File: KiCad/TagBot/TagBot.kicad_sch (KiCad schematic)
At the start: 51 parts, among them IC101 ADXL343BCCZ-RL, J101 Conn_ST_STDC14, J102 Conn_01x06, J103 Conn_01x02, J104 Conn_01x06, J105 Conn_01x02, J106 Conn_01x08, J107 Conn_01x03, J108 Conn_01x03, J109 Conn_01x03, J110 Conn_01x03, J111 Conn_01x04, SW101 SW_Push, SW102 SW_Push, SW103 SW_SPDT_312, U101 STM32G431CBUx, Y101 Crystal

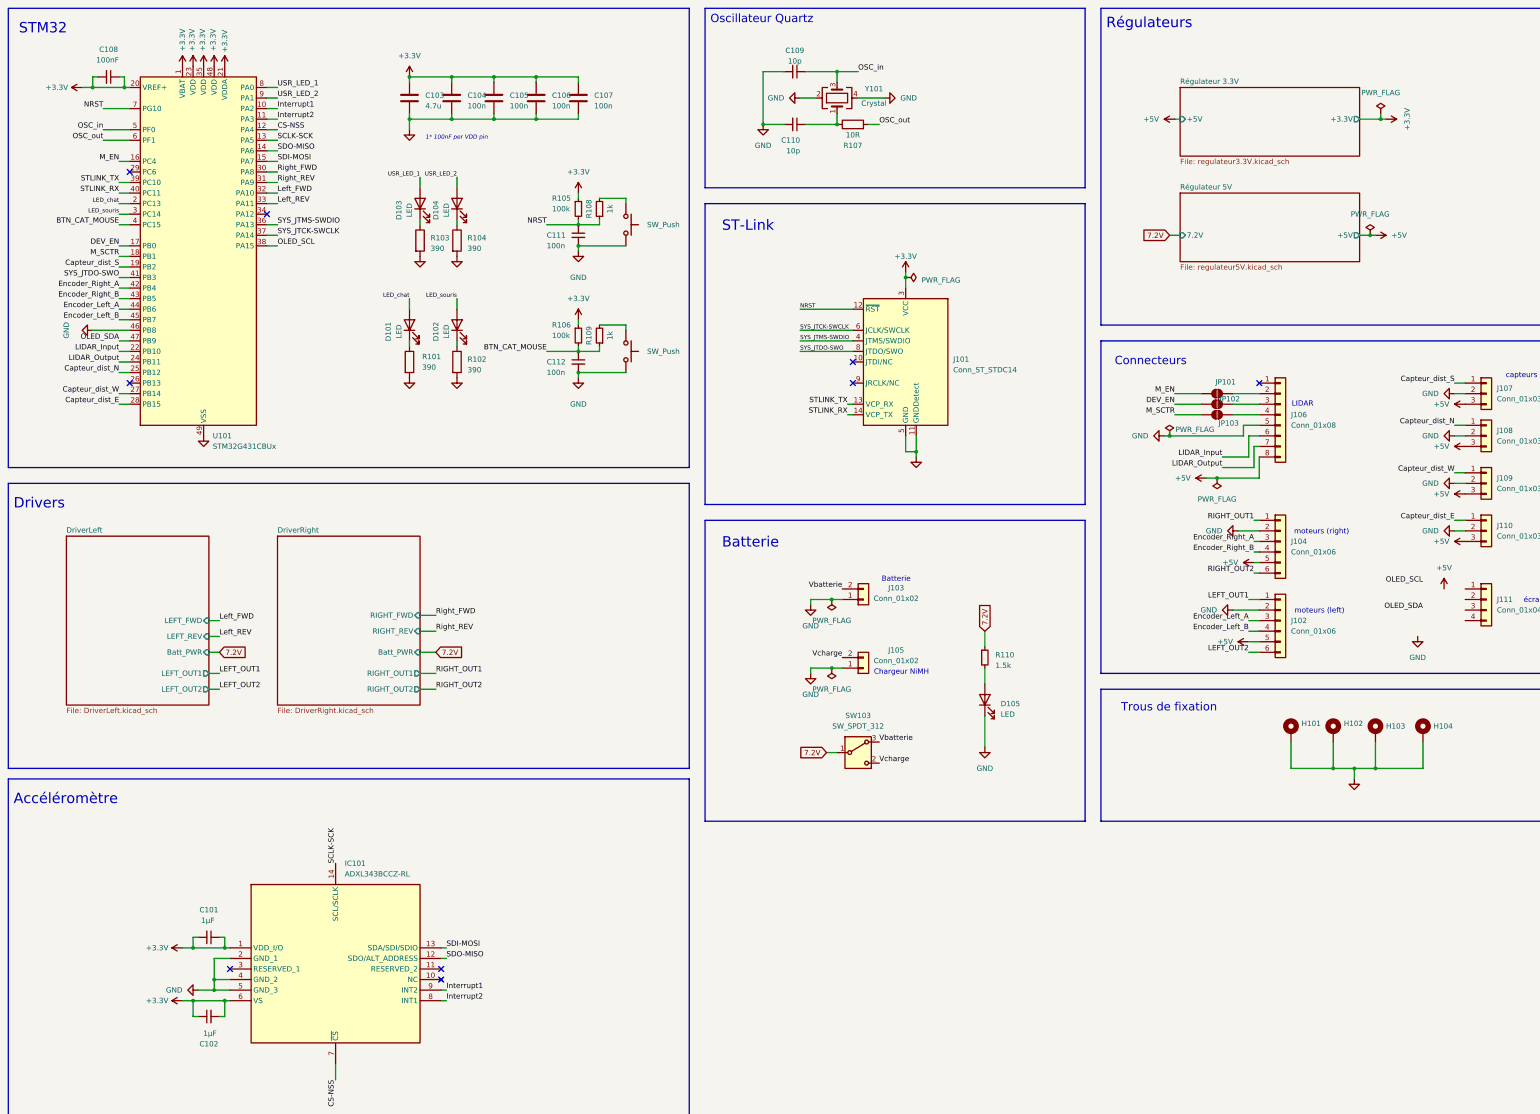
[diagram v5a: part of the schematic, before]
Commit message: update footprint kicad
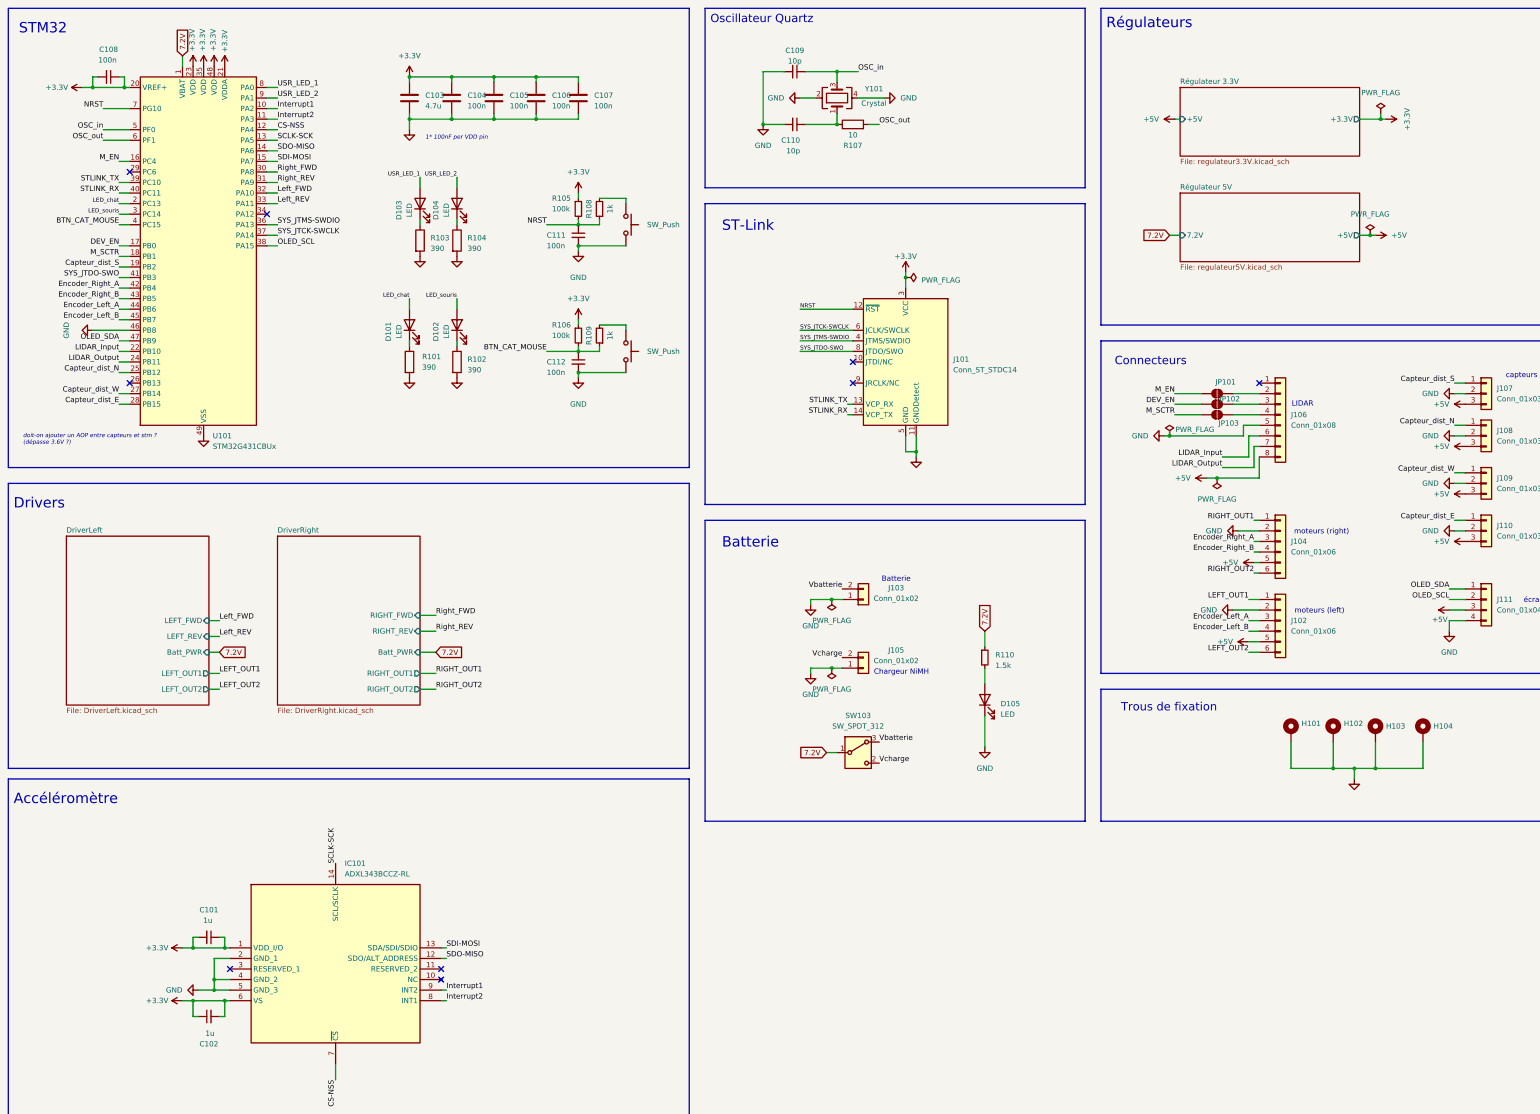
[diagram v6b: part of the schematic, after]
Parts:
- C101, C102: value 1µF -> 1u; footprint (none) -> Capacitor_SMD:C_0402_1005Metric
- C108: value 100nF -> 100n; footprint (none) -> Capacitor_SMD:C_0402_1005Metric
- IC101: footprint ADXL343BCCZRL -> ADXL343BCCZ-RL:ADXL343BCCZRL
- J102, J104: footprint (none) -> Connector_JST:JST_XH_B6B-XH-A_1x06_P2.50mm_Vertical
- J103, J105: footprint Connector_AMASS:AMASS_XT60-F_1x02_P7.20mm_Vertical -> Connector_JST:JST_XH_B2B-XH-A_1x02_P2.50mm_Vertical
- J106: footprint (none) -> Connector_JST:JST_XH_B8B-XH-A_1x08_P2.50mm_Vertical
- J107, J108, J109, J110: footprint (none) -> Connector_JST:JST_XH_B3B-XH-A_1x03_P2.50mm_Vertical
- J111: footprint (none) -> Connector_JST:JST_XH_B4B-XH-A_1x04_P2.50mm_Vertical
- JP101, JP102, JP103: footprint (none) -> Jumper:SolderJumper-2_P1.3mm_Open_TrianglePad1.0x1.5mm
- R107: value 10R -> 10
- SW103: footprint (none) -> wurth_472121020311:472121020311
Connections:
- net +3.3V: no longer U101.1 (VBAT)
- net +5V: now also J111.3 (Pin_3)
- net 7.2V: now also U101.1 (VBAT)
- net GND: now also J111.4 (Pin_4)
- net OLED_SCL: now also J111.2 (Pin_2)
- net OLED_SDA: now also J111.1 (Pin_1)
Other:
- note added: "doit-on ajouter un AOP entre capteurs et stm ? (dépasse 3.6V ?)"
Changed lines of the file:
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@@
 	(wire
 		(pts
+			(xy 361.95 157.48) (xy 365.76 157.48)
+		)
+		(stroke
+			(width 0)
+			(type default)
+		)
+	)
+	(wire
+		(pts
 			(xy 313.69 162.56) (xy 316.23 162.56)
 		)
@@
 	(wire
 		(pts
+			(xy 361.95 160.02) (xy 365.76 160.02)
+		)
+		(stroke
+			(width 0)
+			(type default)
+		)
+	)
+	(wire
+		(pts
 			(xy 132.08 41.91) (xy 132.08 40.64)
 		)
@@
 	(wire
 		(pts
+			(xy 361.95 162.56) (xy 361.95 165.1)
+		)
+		(stroke
+			(width 0)
+			(type default)
+		)
+	)
+	(wire
+		(pts
 			(xy 213.36 157.48) (xy 215.9 157.48)
 		)
@@
 	(wire
 		(pts
+			(xy 57.15 26.67) (xy 57.15 29.21)
+		)
+		(stroke
+			(width 0)
+			(type default)
+		)
+	)
+	(wire
+		(pts
 			(xy 340.36 41.91) (xy 345.44 41.91)
 		)
@@
 	(wire
 		(pts
+			(xy 365.76 162.56) (xy 361.95 162.56)
+		)
+		(stroke
+			(width 0)
+			(type default)
+		)
+	)
+	(wire
+		(pts
 			(xy 363.22 129.54) (xy 365.76 129.54)
 		)
@@
 	(wire
 		(pts
+			(xy 361.95 154.94) (xy 365.76 154.94)
+		)
+		(stroke
+			(width 0)
+			(type default)
+		)
+	)
+	(wire
+		(pts
 			(xy 205.74 92.71) (xy 218.44 92.71)
 		)
@@
 		)
 	)
+	(text "doit-on ajouter un AOP entre capteurs et stm ?\n(dépasse 3.6V ?)"
+		(exclude_from_sim no)
+		(at 18.796 120.396 0)
+		(effects
+			(font
+				(size 1 1)
+				(italic yes)
+			)
+			(justify left bottom)
+		)
+	)
 	(text "Batterie\n"
 		(exclude_from_sim no)
@@
 	)
 	(label "OLED_SCL"
-		(at 355.6 153.67 180)
+		(at 361.95 157.48 180)
 		(fields_autoplaced yes)
 		(effects
@@
 	)
 	(label "OLED_SDA"
-		(at 355.6 160.02 180)
+		(at 361.95 154.94 180)
 		(fields_autoplaced yes)
 		(effects
@@
 	(global_label "7.2V"
 		(shape input)
+		(at 57.15 26.67 90)
+		(fields_autoplaced yes)
+		(effects
+			(font
+				(size 1.27 1.27)
+			)
+			(justify left)
+		)
+		(property "Intersheetrefs" "${INTERSHEET_REFS}"
+			(at 57.15 19.5724 90)
+			(effects
+				(font
+					(size 1.27 1.27)
+				)
+				(justify left)
+				(hide yes)
+			)
+		)
+	)
+	(global_label "7.2V"
+		(shape input)
 		(at 294.64 69.85 180)
 		(fields_autoplaced yes)
@@
 			)
 		)
-		(property "Footprint" "Connector_AMASS:AMASS_XT60-F_1x02_P7.20mm_Vertical"
+		(property "Footprint" "Connector_JST:JST_XH_B2B-XH-A_1x02_P2.50mm_Vertical"
 			(at 220.98 157.48 0)
 			(effects
@@
 		(lib_name "GND_5")
 		(lib_id "power:GND")
-		(at 354.33 166.37 0)
+		(at 361.95 165.1 0)
 		(unit 1)
 		(exclude_from_sim no)
@@
 		(fields_autoplaced yes)
 		(property "Reference" "#PWR0148"
-			(at 354.33 172.72 0)
+			(at 361.95 171.45 0)
 			(effects
 				(font
@@
 		)
 		(property "Value" "GND"
-			(at 354.33 171.45 0)
+			(at 361.95 170.18 0)
 			(effects
 				(font
@@
 		)
 		(property "Footprint" ""
-			(at 354.33 166.37 0)
+			(at 361.95 165.1 0)
 			(effects
 				(font
@@
 		)
 		(property "Datasheet" ""
-			(at 354.33 166.37 0)
+			(at 361.95 165.1 0)
 			(effects
 				(font
@@
 		)
 		(property "Description" "Power symbol creates a global label with name \"GND\" , ground"
-			(at 354.33 166.37 0)
+			(at 361.95 165.1 0)
 			(effects
 				(font
@@
 			)
 		)
-		(property "Footprint" ""
+		(property "Footprint" "Connector_JST:JST_XH_B4B-XH-A_1x04_P2.50mm_Vertical"
 			(at 370.84 157.48 0)
 			(effects
@@
 			)
 		)
-		(property "Value" "1µF"
+		(property "Value" "1u"
 			(at 63.246 234.696 90)
 			(effects
@@
 			)
 		)
-		(property "Footprint" ""
+		(property "Footprint" "Capacitor_SMD:C_0402_1005Metric"
 			(at 63.5 238.76 0)
 			(effects
@@
 	(symbol
 		(lib_id "power:+5V")
-		(at 360.68 154.94 0)
+		(at 361.95 160.02 90)
 		(unit 1)
 		(exclude_from_sim no)
@@
 		(on_board yes)
 		(dnp no)
-		(fields_autoplaced yes)
 		(property "Reference" "#PWR0149"
-			(at 360.68 158.75 0)
+			(at 365.76 160.02 0)
 			(effects
 				(font
@@
 		)
 		(property "Value" "+5V"
-			(at 360.68 149.86 0)
+			(at 359.664 162.306 90)
 			(effects
 				(font
@@
 		)
 		(property "Footprint" ""
-			(at 360.68 154.94 0)
+			(at 361.95 160.02 0)
 			(effects
 				(font
@@
 		)
 		(property "Datasheet" ""
-			(at 360.68 154.94 0)
+			(at 361.95 160.02 0)
 			(effects
 				(font
@@
 		)
 		(property "Description" "Power symbol creates a global label with name \"+5V\""
-			(at 360.68 154.94 0)
+			(at 361.95 160.02 0)
 			(effects
 				(font
@@
 			)
 		)
-		(property "Value" "1µF"
+		(property "Value" "1u"
 			(at 63.754 261.874 90)
 			(effects
@@
 			)
 		)
-		(property "Footprint" ""
+		(property "Footprint" "Capacitor_SMD:C_0402_1005Metric"
 			(at 63.5 257.81 0)
 			(effects
@@
 			)
 		)
-		(property "Footprint" ""
+		(property "Footprint" "Jumper:SolderJumper-2_P1.3mm_Open_TrianglePad1.0x1.5mm"
 			(at 306.07 113.03 0)
 			(effects
@@
 			)
 		)
-		(property "Footprint" ""
+		(property "Footprint" "wurth_472121020311:472121020311"
 			(at 219.71 204.47 0)
 			(effects
@@
 	)
 	(symbol
-		(lib_name "+3.3V_1")
-		(lib_id "power:+3.3V")
-		(at 57.15 29.21 0)
-		(unit 1)
-		(exclude_from_sim no)
-		(in_bom yes)
-		(on_board yes)
-		(dnp no)
-		(property "Reference" "#PWR0102"
-			(at 57.15 33.02 0)
-			(effects
-				(font
-					(size 1.27 1.27)
-				)
-				(hide yes)
-			)
-		)
-		(property "Value" "+3.3V"
-			(at 57.15 22.86 90)
-			(effects
-				(font
-					(size 1.27 1.27)
-				)
-			)
-		)
-		(property "Footprint" ""
-			(at 57.15 29.21 0)
-			(effects
-				(font
-					(size 1.27 1.27)
-				)
-				(hide yes)
-			)
-		)
-		(property "Datasheet" ""
-			(at 57.15 29.21 0)
-			(effects
-				(font
-					(size 1.27 1.27)
-				)
-				(hide yes)
-			)
-		)
-		(property "Description" "Power symbol creates a global label with name \"+3.3V\""
-			(at 57.15 29.21 0)
-			(effects
-				(font
-					(size 1.27 1.27)
-				)
-				(hide yes)
-			)
-		)
-		(pin "1"
-		)
-		(instances
-			(project ""
-				(path "/6db08f37-7cb3-4000-93f1-ba0d0ffbeb19"
-					(reference "#PWR0102")
-					(unit 1)
-				)
-			)
-		)
-	)
-	(symbol
 		(lib_id "power:GND")
 		(at 250.19 193.04 0)
@@
 			)
 		)
-		(property "Footprint" ""
+		(property "Footprint" "Connector_JST:JST_XH_B8B-XH-A_1x08_P2.50mm_Vertical"
 			(at 321.31 113.03 0)
 			(effects
@@
 			)
 		)
-		(property "Footprint" "Connector_AMASS:AMASS_XT60-F_1x02_P7.20mm_Vertical"
+		(property "Footprint" "Connector_JST:JST_XH_B2B-XH-A_1x02_P2.50mm_Vertical"
 			(at 220.98 173.99 0)
 			(effects
@@
 			)
 		)
-		(property "Footprint" ""
+		(property "Footprint" "Jumper:SolderJumper-2_P1.3mm_Open_TrianglePad1.0x1.5mm"
 			(at 306.07 107.95 0)
 			(effects
@@
 			)
 		)
-		(property "Footprint" ""
+		(property "Footprint" "Connector_JST:JST_XH_B3B-XH-A_1x03_P2.50mm_Vertical"
 			(at 370.84 140.97 0)
 			(effects
@@
 			)
 		)
-		(property "Value" "100nF"
+		(property "Value" "100n"
 			(at 39.116 27.686 90)
 			(effects
@@
 			)
 		)
-		(property "Footprint" ""
+		(property "Footprint" "Capacitor_SMD:C_0402_1005Metric"
 			(at 39.37 31.75 0)
 			(effects
@@
 			)
 		)
-		(property "Footprint" ""
+		(property "Footprint" "Jumper:SolderJumper-2_P1.3mm_Open_TrianglePad1.0x1.5mm"
 			(at 306.07 110.49 0)
 			(effects
@@
 			)
 		)
-		(property "Footprint" ""
+		(property "Footprint" "Connector_JST:JST_XH_B3B-XH-A_1x03_P2.50mm_Vertical"
 			(at 370.84 107.95 0)
 			(effects
@@
 			)
 		)
-		(property "Value" "10R"
+		(property "Value" "10"
 			(at 218.44 45.72 90)
 			(effects
@@
 			)
 		)
-		(property "Footprint" ""
+		(property "Footprint" "Connector_JST:JST_XH_B6B-XH-A_1x06_P2.50mm_Vertical"
 			(at 321.31 162.56 0)
 			(effects
@@
 			)
 		)
-		(property "Footprint" ""
+		(property "Footprint" "Connector_JST:JST_XH_B3B-XH-A_1x03_P2.50mm_Vertical"
 			(at 370.84 118.11 0)
 			(effects
@@
 			)
 		)
-		(property "Footprint" "ADXL343BCCZRL"
+		(property "Footprint" "ADXL343BCCZ-RL:ADXL343BCCZRL"
 			(at 115.57 323.52 0)
 			(effects
@@
 					(unit 1)
 				)
+				(path "/6db08f37-7cb3-4000-93f1-ba0d0ffbeb19/285c948d-5578-4bb8-8119-b871ade4552f"
+					(reference "IC101")
+					(unit 1)
+				)
 			)
 		)
@@
 			)
 		)
-		(property "Footprint" ""
+		(property "Footprint" "Connector_JST:JST_XH_B3B-XH-A_1x03_P2.50mm_Vertical"
 			(at 370.84 129.54 0)
 			(effects
@@
 			)
 		)
-		(property "Footprint" ""
+		(property "Footprint" "Connector_JST:JST_XH_B6B-XH-A_1x06_P2.50mm_Vertical"
 			(at 321.31 143.51 0)
 			(effects

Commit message: placement pcb
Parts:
- removed J103: Conn_01x02, Connector_JST:JST_XH_B2B-XH-A_1x02_P2.50mm_Vertical, symbol Connector_Generic:Conn_01x02
- removed J107, J108, J109, J110: Conn_01x03, Connector_JST:JST_XH_B3B-XH-A_1x03_P2.50mm_Vertical, symbol Connector_Generic:Conn_01x03
- removed SW103: SW_SPDT_312, wurth_472121020311:472121020311, symbol Switch:SW_SPDT_312
- added BT101: Battery, Connector_JST:JST_XH_S2B-XH-A_1x02_P2.50mm_Horizontal, symbol Device:Battery
- added J103: Conn_01x03, Connector_JST:JST_XH_S3B-XH-A_1x03_P2.50mm_Horizontal, symbol Connector_Generic:Conn_01x03
- added J107: Conn_01x06, Connector_JST:JST_XH_S6B-XH-A_1x06_P2.50mm_Horizontal, symbol Connector_Generic:Conn_01x06
- D101, D103, D105: reference (none) -> 150060GS55040
- D102: reference (none) -> 150060BS55040
- D104: reference (none) -> 150060RS55040
- J102, J104: footprint Connector_JST:JST_XH_B6B-XH-A_1x06_P2.50mm_Vertical -> Connector_JST:JST_XH_S6B-XH-A_1x06_P2.50mm_Horizontal
- J105: footprint Connector_JST:JST_XH_B2B-XH-A_1x02_P2.50mm_Vertical -> Connector_JST:JST_XH_S2B-XH-A_1x02_P2.50mm_Horizontal
- J106: footprint Connector_JST:JST_XH_B8B-XH-A_1x08_P2.50mm_Vertical -> Connector_JST:JST_XH_S8B-XH-A_1x08_P2.50mm_Horizontal
- J111: footprint Connector_JST:JST_XH_B4B-XH-A_1x04_P2.50mm_Vertical -> Connector_JST:JST_XH_S4B-XH-A_1x04_P2.50mm_Horizontal
- R101: value 390 -> 1.3k
- R102, R103, R104: value 390 -> 100
- R110: value 1.5k -> 4k
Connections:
- net Vcharge is gone; now on net GND: J105.2 (Pin_2)
- net +3.3V: now also U101.1 (VBAT)
- net +5V: now also J107.5 (Pin_5)
- net Capteur_dist_E: now also J107.4 (Pin_4)
- net Capteur_dist_N: now also J107.2 (Pin_2)
- net Capteur_dist_S: now also J107.1 (Pin_1)
- net Capteur_dist_W: now also J107.3 (Pin_3)
- net GND: now also D101.1 (K), D102.1 (K), D103.1 (K), D104.1 (K), BT101.2 (-), J107.6 (Pin_6); no longer J105.1 (Pin_1), R101.2, R102.2, R103.2, R104.2
- net LED_chat: now also R101.2; no longer D101.2 (A)
- net LED_souris: now also R102.2; no longer D102.2 (A)
- net USR_LED_1: now also R103.2; no longer D103.2 (A)
- net USR_LED_2: now also R104.2; no longer D104.2 (A)
- net Vbatterie: now also R110.1, BT101.1 (+), J103.1 (Pin_1)
- net at R103.1: now also D103.2 (A); no longer D103.1 (K)
- net at R101.1: now also D104.2 (A); no longer D101.1 (K)
- net at R104.1: now also D101.2 (A); no longer D104.1 (K)
- net at R102.1: now also D102.2 (A); no longer D102.1 (K)
- removed net 7.2V: R110.1, U101.1 (VBAT)
- net Left_FWD renamed LEFT_FWD
- net Left_REV renamed LEFT_REV
- net Right_FWD renamed RIGHT_FWD
- net Right_REV renamed RIGHT_REV
- new net: J103.3 (Pin_3), J105.1 (Pin_1)
- new net Valim: J103.2 (Pin_2)
- no-connect marks 9 -> 8
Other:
- note added: "Switch"
- moved on the sheet: J105, R101, R102, R103, R104

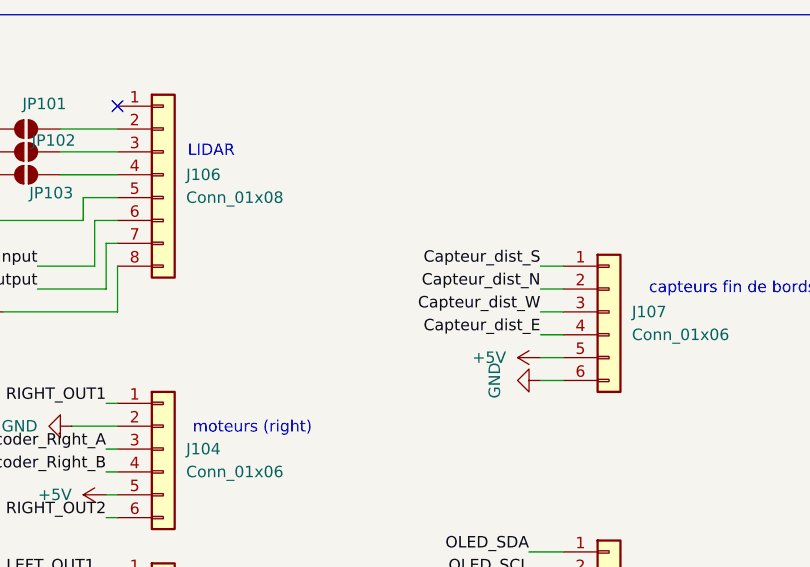
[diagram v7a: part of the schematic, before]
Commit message: ajout résistance capteurs
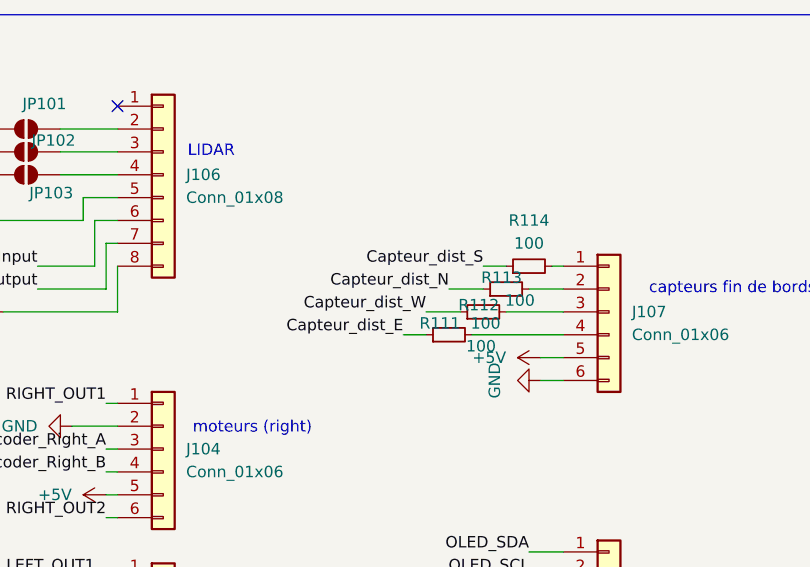
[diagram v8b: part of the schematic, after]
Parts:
- added R111, R112, R113, R114: 100, Resistor_SMD:R_0402_1005Metric, symbol Device:R_Small
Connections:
- net Capteur_dist_E: now also R111.1; no longer J107.4 (Pin_4)
- net Capteur_dist_N: now also R113.1; no longer J107.2 (Pin_2)
- net Capteur_dist_S: now also R114.1; no longer J107.1 (Pin_1)
- net Capteur_dist_W: now also R112.1; no longer J107.3 (Pin_3)
- new net: J107.1 (Pin_1), R114.2
- new net: J107.2 (Pin_2), R113.2
- new net: J107.3 (Pin_3), R112.2
- new net: J107.4 (Pin_4), R111.2
